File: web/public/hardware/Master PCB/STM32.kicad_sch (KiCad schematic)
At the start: 17 parts, among them SW1 nRST, U1 STM32U585VITx

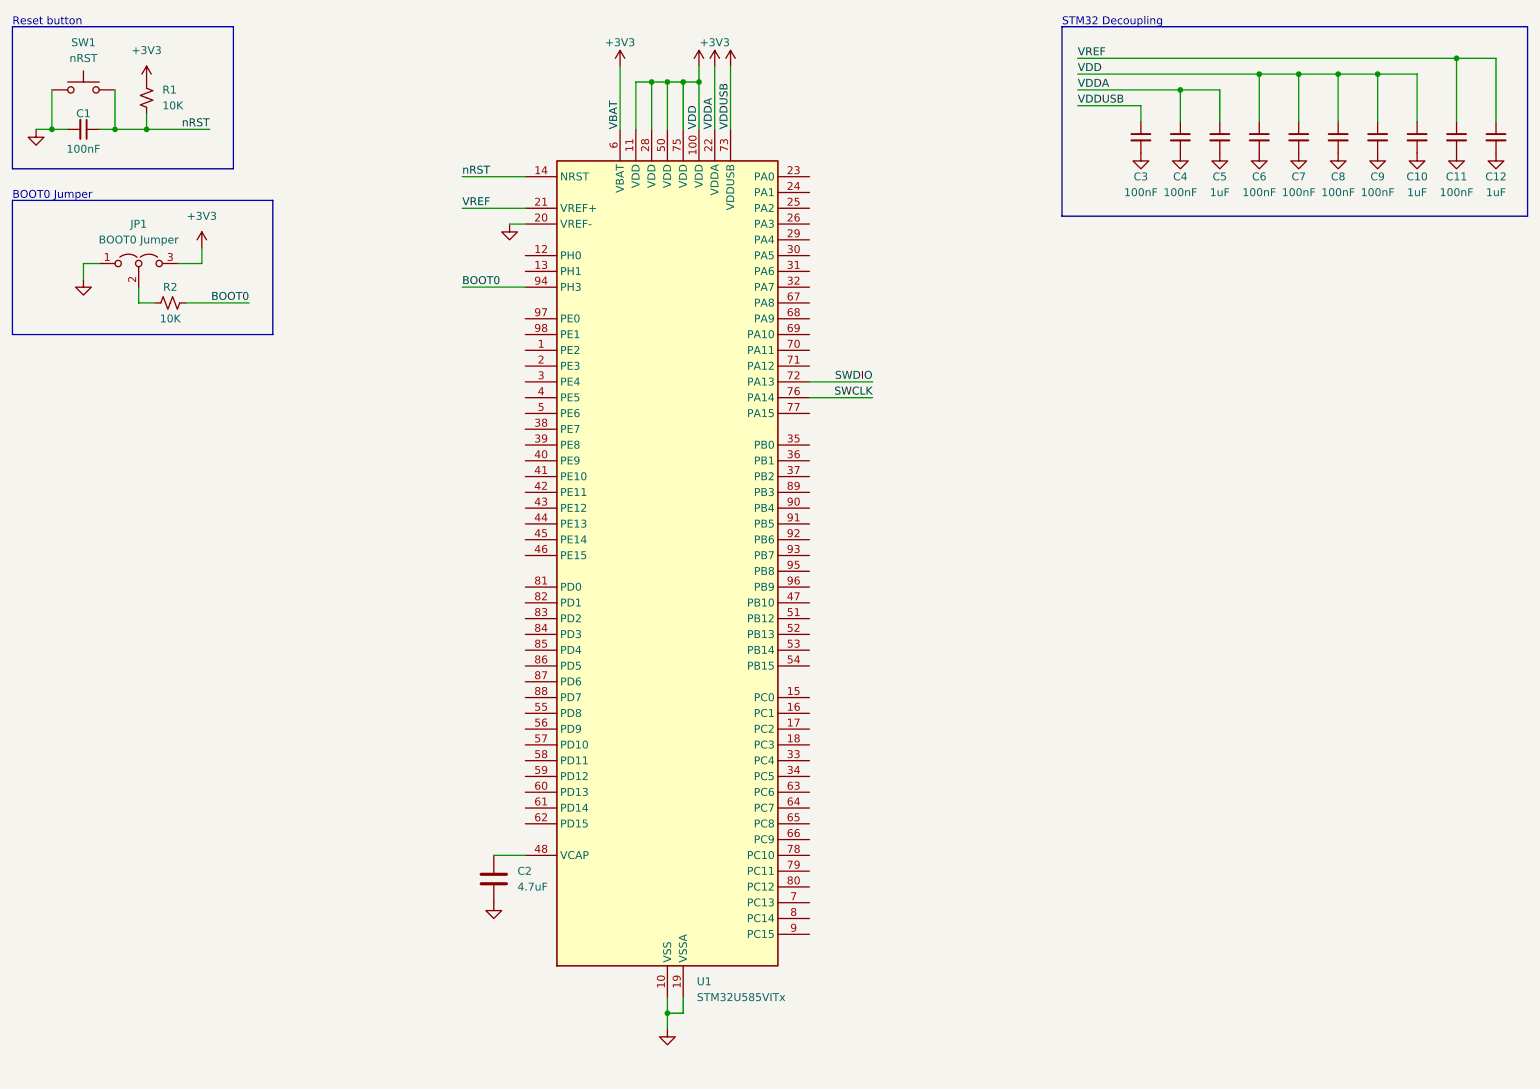
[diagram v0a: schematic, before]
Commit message: Finish schematic and start routing PCB
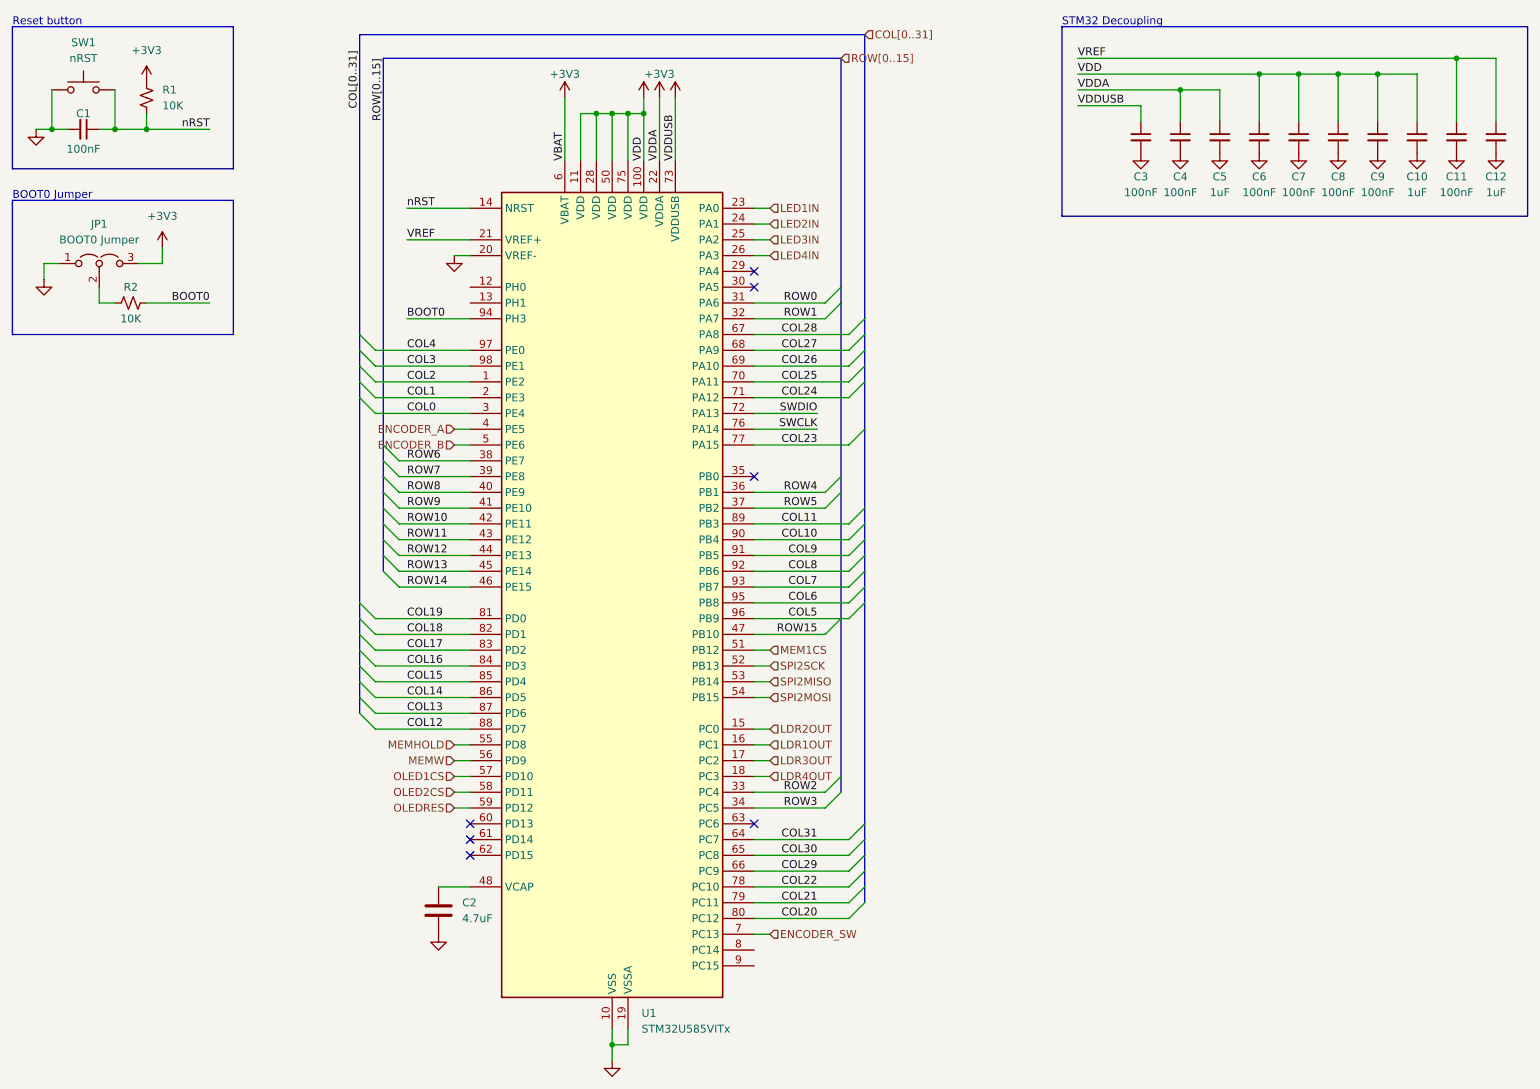
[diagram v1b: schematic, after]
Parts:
- C1, C10, C11, C12, C2, C3, C4, C5, C6, C7, C8, C9: footprint (none) -> Capacitor_SMD:C_0805_2012Metric_Pad1.18x1.45mm_HandSolder
- JP1: footprint (none) -> Connector_PinHeader_2.54mm:PinHeader_1x03_P2.54mm_Vertical
- R1, R2: footprint (none) -> Resistor_SMD:R_0805_2012Metric_Pad1.20x1.40mm_HandSolder
- SW1: footprint (none) -> Button_Switch_THT:SW_PUSH_6mm
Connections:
- net COL2: now reaches U1.1 (PE2)
- net LDR2OUT: now reaches U1.15 (PC0)
- net LDR1OUT: now reaches U1.16 (PC1)
- net LDR3OUT: now reaches U1.17 (PC2)
- net LDR4OUT: now reaches U1.18 (PC3)
- net COL1: now reaches U1.2 (PE3)
- net LED1IN: now reaches U1.23 (PA0)
- net LED2IN: now reaches U1.24 (PA1)
- net LED3IN: now reaches U1.25 (PA2)
- net LED4IN: now reaches U1.26 (PA3)
- net COL0: now reaches U1.3 (PE4)
- net ROW0: now reaches U1.31 (PA6)
- net ROW1: now reaches U1.32 (PA7)
- net ROW2: now reaches U1.33 (PC4)
- net ROW3: now reaches U1.34 (PC5)
- net ROW4: now reaches U1.36 (PB1)
- net ROW5: now reaches U1.37 (PB2)
- net ROW6: now reaches U1.38 (PE7)
- net ROW7: now reaches U1.39 (PE8)
- net ENCODER_A: now reaches U1.4 (PE5)
- net ROW8: now reaches U1.40 (PE9)
- net ROW9: now reaches U1.41 (PE10)
- net ROW10: now reaches U1.42 (PE11)
- net ROW11: now reaches U1.43 (PE12)
- net ROW12: now reaches U1.44 (PE13)
- net ROW13: now reaches U1.45 (PE14)
- net ROW14: now reaches U1.46 (PE15)
- net ROW15: now reaches U1.47 (PB10)
- net ENCODER_B: now reaches U1.5 (PE6)
- net MEM1CS: now reaches U1.51 (PB12)
- net SPI2SCK: now reaches U1.52 (PB13)
- net SPI2MISO: now reaches U1.53 (PB14)
- net SPI2MOSI: now reaches U1.54 (PB15)
- net MEMHOLD: now reaches U1.55 (PD8)
- net MEMW: now reaches U1.56 (PD9)
- net OLED1CS: now reaches U1.57 (PD10)
- net OLED2CS: now reaches U1.58 (PD11)
- net OLEDRES: now reaches U1.59 (PD12)
- net COL31: now reaches U1.64 (PC7)
- net COL30: now reaches U1.65 (PC8)
- net COL29: now reaches U1.66 (PC9)
- net COL28: now reaches U1.67 (PA8)
- net COL27: now reaches U1.68 (PA9)
- net COL26: now reaches U1.69 (PA10)
- net ENCODER_SW: now reaches U1.7 (PC13)
- net COL25: now reaches U1.70 (PA11)
- net COL24: now reaches U1.71 (PA12)
- net COL23: now reaches U1.77 (PA15)
- net COL22: now reaches U1.78 (PC10)
- net COL21: now reaches U1.79 (PC11)
- net COL20: now reaches U1.80 (PC12)
- net COL19: now reaches U1.81 (PD0)
- net COL18: now reaches U1.82 (PD1)
- net COL17: now reaches U1.83 (PD2)
- net COL16: now reaches U1.84 (PD3)
- net COL15: now reaches U1.85 (PD4)
- net COL14: now reaches U1.86 (PD5)
- net COL13: now reaches U1.87 (PD6)
- net COL12: now reaches U1.88 (PD7)
- net COL11: now reaches U1.89 (PB3)
- net COL10: now reaches U1.90 (PB4)
- net COL9: now reaches U1.91 (PB5)
- net COL8: now reaches U1.92 (PB6)
- net COL7: now reaches U1.93 (PB7)
- net COL6: now reaches U1.95 (PB8)
- net COL5: now reaches U1.96 (PB9)
- net COL4: now reaches U1.97 (PE0)
- net COL3: now reaches U1.98 (PE1)
- no-connect marks 0 -> 7
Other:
- moved on the sheet: C2, JP1, R2, U1

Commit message: Route lots
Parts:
- added C9: 100nF, Capacitor_SMD:C_0805_2012Metric_Pad1.18x1.45mm_HandSolder, symbol Device:C_Small
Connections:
- net +3V3: now also C9.1
- net GND: now also C9.2
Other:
- moved on the sheet: C3, C4, C5, C6, C7, C8, C9

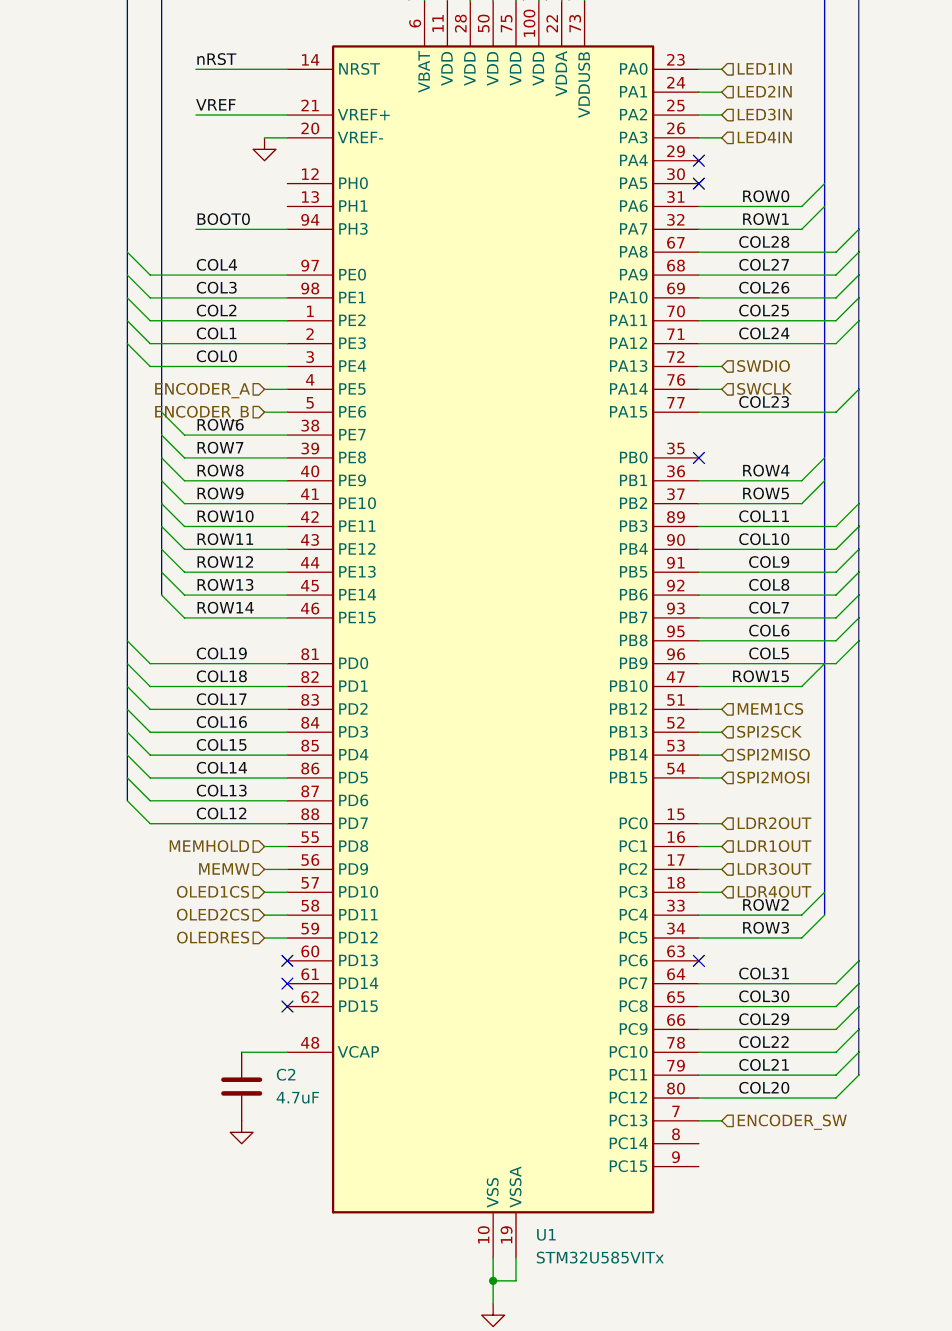
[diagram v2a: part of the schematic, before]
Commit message: Add missing signals to master PCB for relay and OLED DC, add mounting holes, add text, add dimensions
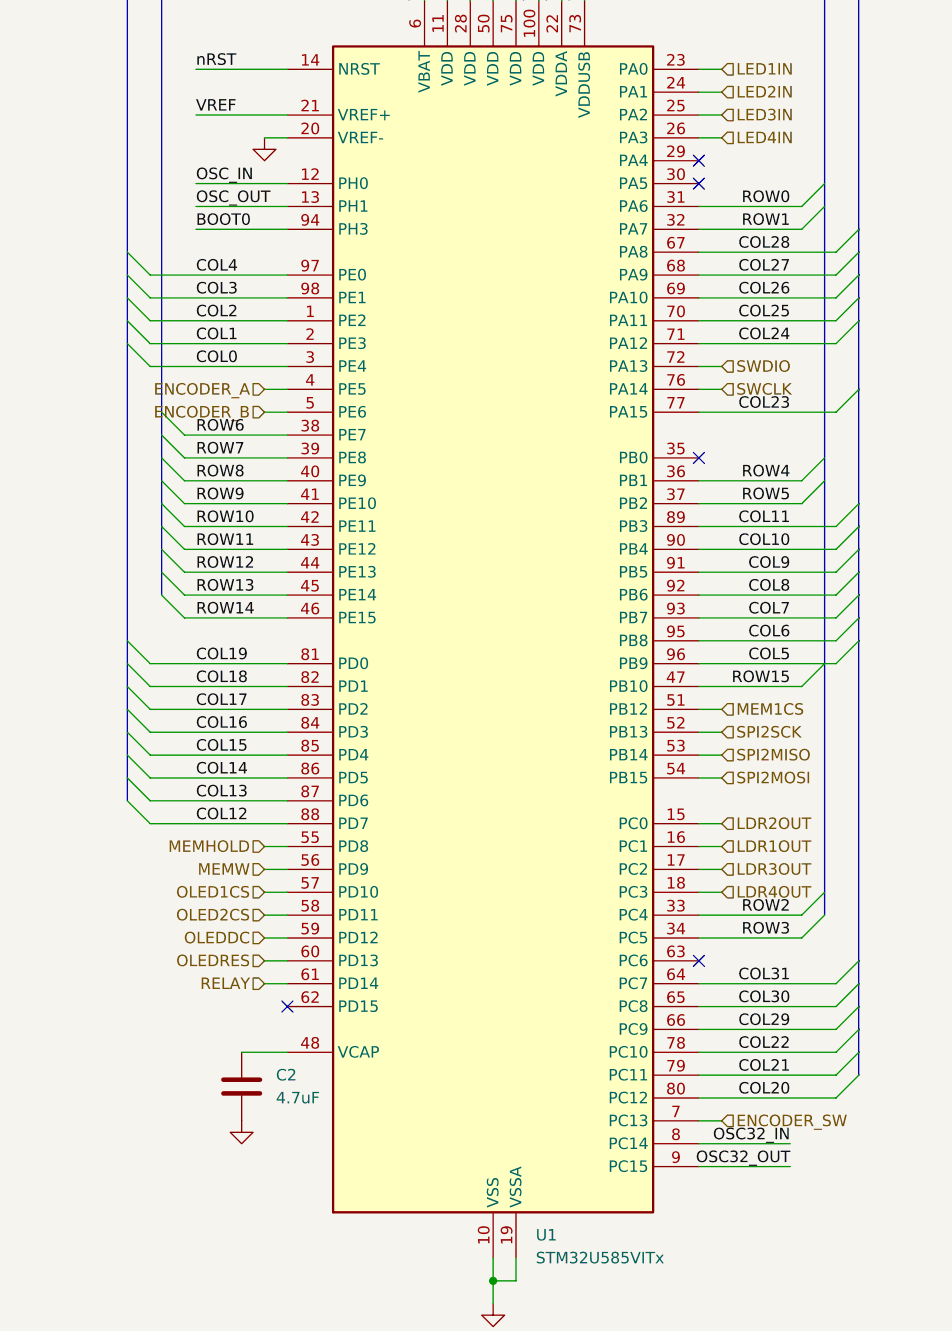
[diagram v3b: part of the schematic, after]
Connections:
- net OLEDRES: now also U1.60 (PD13); no longer U1.59 (PD12)
- net OSC_IN: now reaches U1.12 (PH0)
- net OSC_OUT: now reaches U1.13 (PH1)
- net RELAY: now reaches U1.61 (PD14)
- net OSC32_IN: now reaches U1.8 (PC14)
- net OSC32_OUT: now reaches U1.9 (PC15)
- new net OLEDDC: U1.59 (PD12)
- no-connect marks 7 -> 5
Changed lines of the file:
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@@
   (no_connect (at 137.16 90.17))
   (no_connect (at 137.16 146.05))
-  (no_connect (at 91.44 146.05))
   (no_connect (at 91.44 151.13))
-  (no_connect (at 91.44 148.59))
   (bus_entry (at 73.66 128.27) (size 2.54 2.54)
     (stroke (width 0) (type default))
@@
     (stroke (width 0) (type default))
   )
+  (wire (pts (xy 88.9 148.59) (xy 91.44 148.59))
+    (stroke (width 0) (type default))
+  )
   (bus (pts (xy 151.13 113.03) (xy 151.13 138.43))
     (stroke (width 0) (type default))
@@
     (stroke (width 0) (type default))
   )
+  (wire (pts (xy 137.16 168.91) (xy 147.32 168.91))
+    (stroke (width 0) (type default))
+  )
   (bus (pts (xy 73.66 69.85) (xy 73.66 72.39))
     (stroke (width 0) (type default))
@@
     (stroke (width 0) (type default))
   )
+  (wire (pts (xy 81.28 59.69) (xy 91.44 59.69))
+    (stroke (width 0) (type default))
+  )
   (wire (pts (xy 137.16 161.29) (xy 152.4 161.29))
     (stroke (width 0) (type default))
@@
     (stroke (width 0) (type default))
   )
+  (wire (pts (xy 88.9 146.05) (xy 91.44 146.05))
+    (stroke (width 0) (type default))
+  )
   (wire (pts (xy 137.16 97.79) (xy 152.4 97.79))
     (stroke (width 0) (type default))
@@
     (stroke (width 0) (type default))
   )
+  (wire (pts (xy 81.28 62.23) (xy 91.44 62.23))
+    (stroke (width 0) (type default))
+  )
   (wire (pts (xy 76.2 115.57) (xy 91.44 115.57))
     (stroke (width 0) (type default))
   )
+  (wire (pts (xy 137.16 166.37) (xy 147.32 166.37))
+    (stroke (width 0) (type default))
+  )
   (wire (pts (xy 88.9 143.51) (xy 91.44 143.51))
     (stroke (width 0) (type default))
@@
     (effects (font (size 1.27 1.27)) (justify left bottom))
   )
+  (label "OSC32_IN" (at 147.32 166.37 180) (fields_autoplaced)
+    (effects (font (size 1.27 1.27)) (justify right bottom))
+  )
   (label "COL26" (at 147.32 72.39 180) (fields_autoplaced)
     (effects (font (size 1.27 1.27)) (justify right bottom))
@@
     (effects (font (size 1.27 1.27)) (justify right bottom))
   )
+  (label "OSC32_OUT" (at 147.32 168.91 180) (fields_autoplaced)
+    (effects (font (size 1.27 1.27)) (justify right bottom))
+  )
   (label "ROW0" (at 147.32 62.23 180) (fields_autoplaced)
     (effects (font (size 1.27 1.27)) (justify right bottom))
@@
     (effects (font (size 1.27 1.27)) (justify right bottom))
   )
+  (label "OSC_IN" (at 81.28 59.69 0) (fields_autoplaced)
+    (effects (font (size 1.27 1.27)) (justify left bottom))
+  )
   (label "COL11" (at 147.32 97.79 180) (fields_autoplaced)
     (effects (font (size 1.27 1.27)) (justify right bottom))
@@
   (label "ROW4" (at 147.32 92.71 180) (fields_autoplaced)
     (effects (font (size 1.27 1.27)) (justify right bottom))
+  )
+  (label "OSC_OUT" (at 81.28 62.23 0) (fields_autoplaced)
+    (effects (font (size 1.27 1.27)) (justify left bottom))
   )
   (label "ROW15" (at 147.32 115.57 180) (fields_autoplaced)
@@
     (effects (font (size 1.27 1.27)) (justify left))
   )
+  (hierarchical_label "RELAY" (shape input) (at 88.9 148.59 180) (fields_autoplaced)
+    (effects (font (size 1.27 1.27)) (justify right))
+  )
   (hierarchical_label "COL[0..31]" (shape input) (at 154.94 19.05 0) (fields_autoplaced)
     (effects (font (size 1.27 1.27)) (justify left))
@@
     (effects (font (size 1.27 1.27)) (justify left))
   )
+  (hierarchical_label "OLEDDC" (shape input) (at 88.9 143.51 180) (fields_autoplaced)
+    (effects (font (size 1.27 1.27)) (justify right))
+  )
   (hierarchical_label "SPI2MOSI" (shape input) (at 139.7 125.73 0) (fields_autoplaced)
     (effects (font (size 1.27 1.27)) (justify left))
@@
     (effects (font (size 1.27 1.27)) (justify left))
   )
-  (hierarchical_label "OLEDRES" (shape input) (at 88.9 143.51 180) (fields_autoplaced)
+  (hierarchical_label "OLEDRES" (shape input) (at 88.9 146.05 180) (fields_autoplaced)
     (effects (font (size 1.27 1.27)) (justify right))
   )
